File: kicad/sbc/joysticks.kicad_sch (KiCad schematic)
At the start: 8 parts, among them U28 7400, U29 74LS244, U7 74125

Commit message: io area relayout
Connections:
- net at Port1.1, U29.11 (I0b): now also RR1.5; no longer RR1.2
- net at Port1.6 (P6), U7.2 (D): now also RR1.6; no longer RR1.3
- net at Port1.2, U29.13 (I1b): now also RR1.7; no longer RR1.4
- net at Port1.3, U29.15 (I2b): now also RR1.8; no longer RR1.5
- net at Port1.4, U29.17 (I3b): now also RR1.9; no longer RR1.6
- net at Port2.2, U29.4 (I1a): now also RR1.2; no longer RR1.7
- net at Port2.3, U29.6 (I2a): now also RR1.3; no longer RR1.8
- net at Port2.4, U29.8 (I3a): now also RR1.4; no longer RR1.9
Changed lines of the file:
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@@
 (kicad_sch (version 20230121) (generator eeschema)
   (paper "A4")
-  (junction (at 214.63 85.09) (diameter 0) (color 0 0 0 0)
-  )
-  (junction (at 222.25 74.93) (diameter 0) (color 0 0 0 0)
+  (junction (at 229.87 74.93) (diameter 0) (color 0 0 0 0)
+  )
+  (junction (at 214.63 118.11) (diameter 0) (color 0 0 0 0)
+  )
+  (junction (at 219.71 107.95) (diameter 0) (color 0 0 0 0)
+  )
+  (junction (at 232.41 69.85) (diameter 0) (color 0 0 0 0)
   )
   (junction (at 185.42 74.93) (diameter 0) (color 0 0 0 0)
@@
   (junction (at 133.35 72.39) (diameter 0) (color 0 0 0 0)
   )
-  (junction (at 232.41 107.95) (diameter 0) (color 0 0 0 0)
+  (junction (at 222.25 85.09) (diameter 0) (color 0 0 0 0)
   )
   (junction (at 214.63 123.19) (diameter 0) (color 0 0 0 0)
   )
-  (junction (at 224.79 69.85) (diameter 0) (color 0 0 0 0)
+  (junction (at 227.33 80.01) (diameter 0) (color 0 0 0 0)
   )
   (junction (at 217.17 120.65) (diameter 0) (color 0 0 0 0)
   )
-  (junction (at 227.33 118.11) (diameter 0) (color 0 0 0 0)
-  )
-  (junction (at 229.87 113.03) (diameter 0) (color 0 0 0 0)
-  )
   (junction (at 142.24 107.95) (diameter 0) (color 0 0 0 0)
   )
   (junction (at 209.55 77.47) (diameter 0) (color 0 0 0 0)
   )
+  (junction (at 217.17 113.03) (diameter 0) (color 0 0 0 0)
+  )
   (junction (at 74.93 88.9) (diameter 0) (color 0 0 0 0)
   )
+  (junction (at 224.79 82.55) (diameter 0) (color 0 0 0 0)
+  )
   (junction (at 209.55 62.23) (diameter 0) (color 0 0 0 0)
   )
@@
   (junction (at 137.16 102.87) (diameter 0) (color 0 0 0 0)
   )
-  (junction (at 219.71 80.01) (diameter 0) (color 0 0 0 0)
-  )
   (junction (at 209.55 115.57) (diameter 0) (color 0 0 0 0)
-  )
-  (junction (at 217.17 82.55) (diameter 0) (color 0 0 0 0)
   )
   (junction (at 40.64 96.52) (diameter 0) (color 0 0 0 0)
@@
   (no_connect (at 257.81 102.87))
   (no_connect (at 257.81 64.77))
-  (wire (pts (xy 229.87 60.96) (xy 229.87 113.03))
-    (stroke (width 0) (type default))
-  )
-  (wire (pts (xy 224.79 60.96) (xy 224.79 69.85))
+  (wire (pts (xy 232.41 60.96) (xy 232.41 69.85))
     (stroke (width 0) (type default))
   )
@@
     (stroke (width 0) (type default))
   )
-  (wire (pts (xy 222.25 74.93) (xy 257.81 74.93))
-    (stroke (width 0) (type default))
-  )
   (wire (pts (xy 191.77 92.71) (xy 182.88 92.71))
     (stroke (width 0) (type default))
   )
-  (wire (pts (xy 203.2 85.09) (xy 214.63 85.09))
-    (stroke (width 0) (type default))
-  )
   (wire (pts (xy 40.64 80.01) (xy 76.2 80.01))
     (stroke (width 0) (type default))
   )
-  (wire (pts (xy 219.71 60.96) (xy 219.71 80.01))
+  (wire (pts (xy 227.33 60.96) (xy 227.33 80.01))
     (stroke (width 0) (type default))
   )
@@
     (stroke (width 0) (type default))
   )
+  (wire (pts (xy 224.79 60.96) (xy 224.79 82.55))
+    (stroke (width 0) (type default))
+  )
   (wire (pts (xy 133.35 123.19) (xy 133.35 72.39))
     (stroke (width 0) (type default))
@@
     (stroke (width 0) (type default))
   )
-  (wire (pts (xy 219.71 80.01) (xy 257.81 80.01))
+  (wire (pts (xy 232.41 69.85) (xy 257.81 69.85))
     (stroke (width 0) (type default))
   )
@@
     (stroke (width 0) (type default))
   )
-  (wire (pts (xy 189.23 82.55) (xy 217.17 82.55))
+  (wire (pts (xy 189.23 82.55) (xy 224.79 82.55))
     (stroke (width 0) (type default))
   )
@@
     (stroke (width 0) (type default))
   )
+  (wire (pts (xy 214.63 60.96) (xy 214.63 118.11))
+    (stroke (width 0) (type default))
+  )
   (wire (pts (xy 182.88 102.87) (xy 203.2 102.87))
     (stroke (width 0) (type default))
@@
     (stroke (width 0) (type default))
   )
-  (wire (pts (xy 195.58 74.93) (xy 222.25 74.93))
+  (wire (pts (xy 195.58 74.93) (xy 229.87 74.93))
     (stroke (width 0) (type default))
   )
@@
     (stroke (width 0) (type default))
   )
-  (wire (pts (xy 224.79 69.85) (xy 257.81 69.85))
-    (stroke (width 0) (type default))
-  )
-  (wire (pts (xy 195.58 118.11) (xy 227.33 118.11))
+  (wire (pts (xy 195.58 118.11) (xy 214.63 118.11))
     (stroke (width 0) (type default))
   )
@@
     (stroke (width 0) (type default))
   )
-  (wire (pts (xy 232.41 60.96) (xy 232.41 107.95))
-    (stroke (width 0) (type default))
-  )
   (wire (pts (xy 106.68 58.42) (xy 185.42 58.42))
     (stroke (width 0) (type default))
   )
-  (wire (pts (xy 229.87 113.03) (xy 257.81 113.03))
-    (stroke (width 0) (type default))
-  )
   (wire (pts (xy 106.68 82.55) (xy 106.68 58.42))
     (stroke (width 0) (type default))
@@
     (stroke (width 0) (type default))
   )
-  (wire (pts (xy 227.33 60.96) (xy 227.33 118.11))
+  (wire (pts (xy 224.79 82.55) (xy 257.81 82.55))
     (stroke (width 0) (type default))
   )
@@
     (stroke (width 0) (type default))
   )
-  (wire (pts (xy 217.17 82.55) (xy 257.81 82.55))
-    (stroke (width 0) (type default))
-  )
   (wire (pts (xy 176.53 74.93) (xy 185.42 74.93))
     (stroke (width 0) (type default))
   )
+  (wire (pts (xy 229.87 74.93) (xy 257.81 74.93))
+    (stroke (width 0) (type default))
+  )
   (wire (pts (xy 217.17 120.65) (xy 217.17 134.62))
     (stroke (width 0) (type default))
   )
+  (wire (pts (xy 227.33 80.01) (xy 257.81 80.01))
+    (stroke (width 0) (type default))
+  )
   (wire (pts (xy 209.55 77.47) (xy 257.81 77.47))
     (stroke (width 0) (type default))
@@
     (stroke (width 0) (type default))
   )
-  (wire (pts (xy 214.63 60.96) (xy 214.63 85.09))
-    (stroke (width 0) (type default))
-  )
   (wire (pts (xy 182.88 100.33) (xy 203.2 100.33))
     (stroke (width 0) (type default))
@@
     (stroke (width 0) (type default))
   )
-  (wire (pts (xy 222.25 60.96) (xy 222.25 74.93))
+  (wire (pts (xy 229.87 60.96) (xy 229.87 74.93))
     (stroke (width 0) (type default))
   )
@@
     (stroke (width 0) (type default))
   )
-  (wire (pts (xy 203.2 107.95) (xy 232.41 107.95))
+  (wire (pts (xy 203.2 107.95) (xy 219.71 107.95))
     (stroke (width 0) (type default))
   )
@@
     (stroke (width 0) (type default))
   )
+  (wire (pts (xy 222.25 85.09) (xy 257.81 85.09))
+    (stroke (width 0) (type default))
+  )
   (wire (pts (xy 118.11 107.95) (xy 142.24 107.95))
     (stroke (width 0) (type default))
@@
     (stroke (width 0) (type default))
   )
+  (wire (pts (xy 222.25 60.96) (xy 222.25 85.09))
+    (stroke (width 0) (type default))
+  )
   (wire (pts (xy 199.39 105.41) (xy 182.88 105.41))
     (stroke (width 0) (type default))
@@
     (stroke (width 0) (type default))
   )
-  (wire (pts (xy 214.63 85.09) (xy 257.81 85.09))
+  (wire (pts (xy 219.71 107.95) (xy 257.81 107.95))
+    (stroke (width 0) (type default))
+  )
+  (wire (pts (xy 214.63 118.11) (xy 257.81 118.11))
+    (stroke (width 0) (type default))
+  )
+  (wire (pts (xy 203.2 85.09) (xy 222.25 85.09))
     (stroke (width 0) (type default))
   )
@@
     (stroke (width 0) (type default))
   )
-  (wire (pts (xy 232.41 107.95) (xy 257.81 107.95))
-    (stroke (width 0) (type default))
-  )
   (wire (pts (xy 185.42 125.73) (xy 185.42 134.62))
     (stroke (width 0) (type default))
   )
+  (wire (pts (xy 219.71 60.96) (xy 219.71 107.95))
+    (stroke (width 0) (type default))
+  )
   (wire (pts (xy 147.32 97.79) (xy 142.24 97.79))
     (stroke (width 0) (type default))
   )
-  (wire (pts (xy 227.33 118.11) (xy 257.81 118.11))
-    (stroke (width 0) (type default))
-  )
   (wire (pts (xy 191.77 123.19) (xy 214.63 123.19))
     (stroke (width 0) (type default))
   )
-  (wire (pts (xy 199.39 113.03) (xy 229.87 113.03))
-    (stroke (width 0) (type default))
-  )
-  (wire (pts (xy 199.39 80.01) (xy 219.71 80.01))
-    (stroke (width 0) (type default))
-  )
-  (wire (pts (xy 191.77 69.85) (xy 224.79 69.85))
-    (stroke (width 0) (type default))
-  )
-  (wire (pts (xy 217.17 60.96) (xy 217.17 82.55))
+  (wire (pts (xy 199.39 113.03) (xy 217.17 113.03))
+    (stroke (width 0) (type default))
+  )
+  (wire (pts (xy 217.17 60.96) (xy 217.17 113.03))
+    (stroke (width 0) (type default))
+  )
+  (wire (pts (xy 199.39 80.01) (xy 227.33 80.01))
+    (stroke (width 0) (type default))
+  )
+  (wire (pts (xy 191.77 69.85) (xy 232.41 69.85))
     (stroke (width 0) (type default))
   )
@@
   )
   (wire (pts (xy 118.11 102.87) (xy 137.16 102.87))
+    (stroke (width 0) (type default))
+  )
+  (wire (pts (xy 217.17 113.03) (xy 257.81 113.03))
     (stroke (width 0) (type default))
   )
@@
     )
     (property "Footprint" "Resistor_THT:R_Array_SIP8" (at 223.52 52.07 0)
-      (effects (font (size 1.27 1.27)))
+      (effects (font (size 1.27 1.27)) hide)
     )
     (property "Datasheet" "" (at 223.52 52.07 0)

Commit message: routing
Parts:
- added unit 5 of U28
- Port1, Port2: symbol io-rescue:DB9 -> Connector:DE9_Plug_MountingHoles
- R41, R42: symbol io-rescue:R -> Device:R
- RR1: footprint Resistor_THT:R_Array_SIP8 -> Resistor_THT:R_Array_SIP9; symbol io-rescue:RR8 -> Device:R_Network08
- U28: symbol io-rescue:7400 -> 74xx:7400
- U29: symbol io-rescue:74LS244 -> 74xx:74LS244
- U7: symbol io-rescue:74125 -> 74xx_IEEE:74125
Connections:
- net GND: now also Port1.0 (PAD), Port2.0 (PAD), U29.20 (VCC), U28.7 (GND); no longer U28.7 (GND), U28.7 (GND), U28.7 (GND), U29.10 (GND)
- net VCC: now also U29.10 (GND), U28.14 (VCC); no longer U28.14 (VCC), U28.14 (VCC), U28.14 (VCC), U29.20 (VCC)

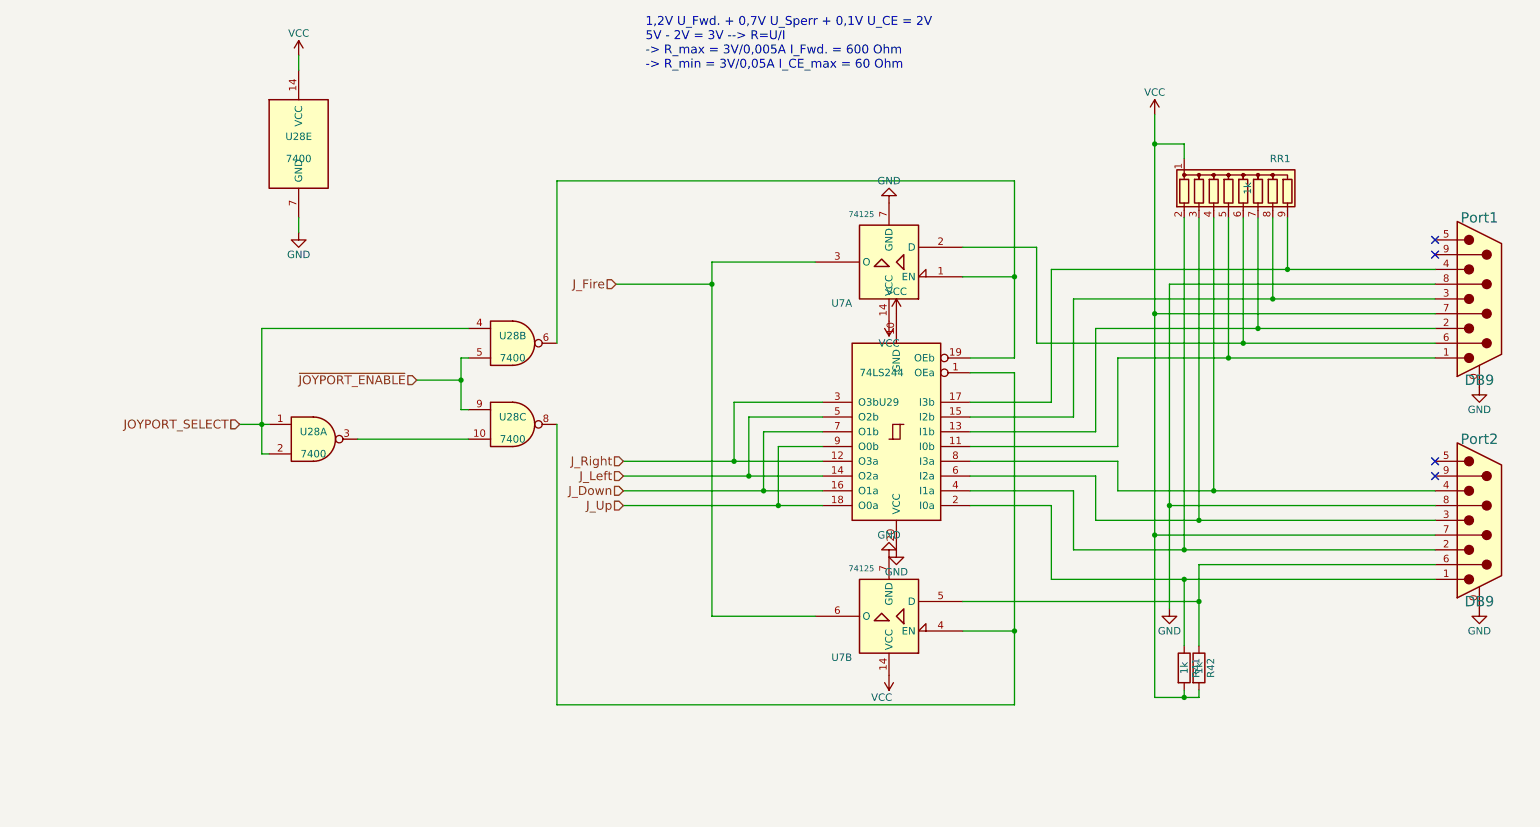
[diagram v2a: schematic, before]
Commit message: fix mixup of vcc and gnd at the 74244
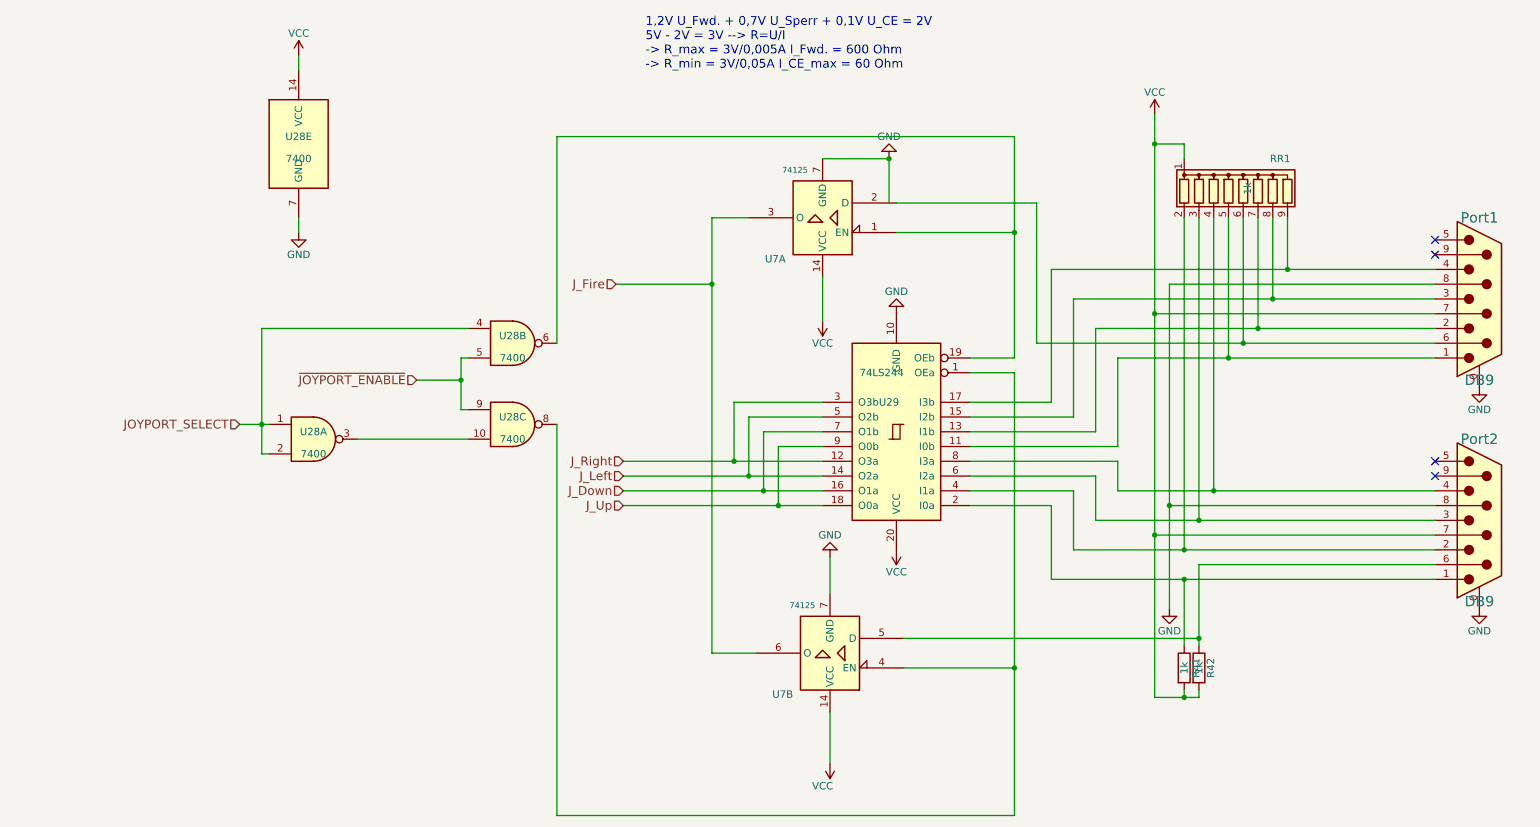
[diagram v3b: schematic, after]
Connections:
- net GND: now also U29.10 (GND); no longer U29.20 (VCC)
- net VCC: now also U29.20 (VCC); no longer U29.10 (GND)
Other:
- moved on the sheet: U7A, U7B
